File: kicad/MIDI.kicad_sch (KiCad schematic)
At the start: 24 parts, among them J11 AudioJack2, J12 AudioJack2, J13 AudioJack2, J5 DIN-5_180degree, J6 DIN-5_180degree, J7 DIN-5_180degree, J9 Conn_01x07_Socket, U5 H11L1

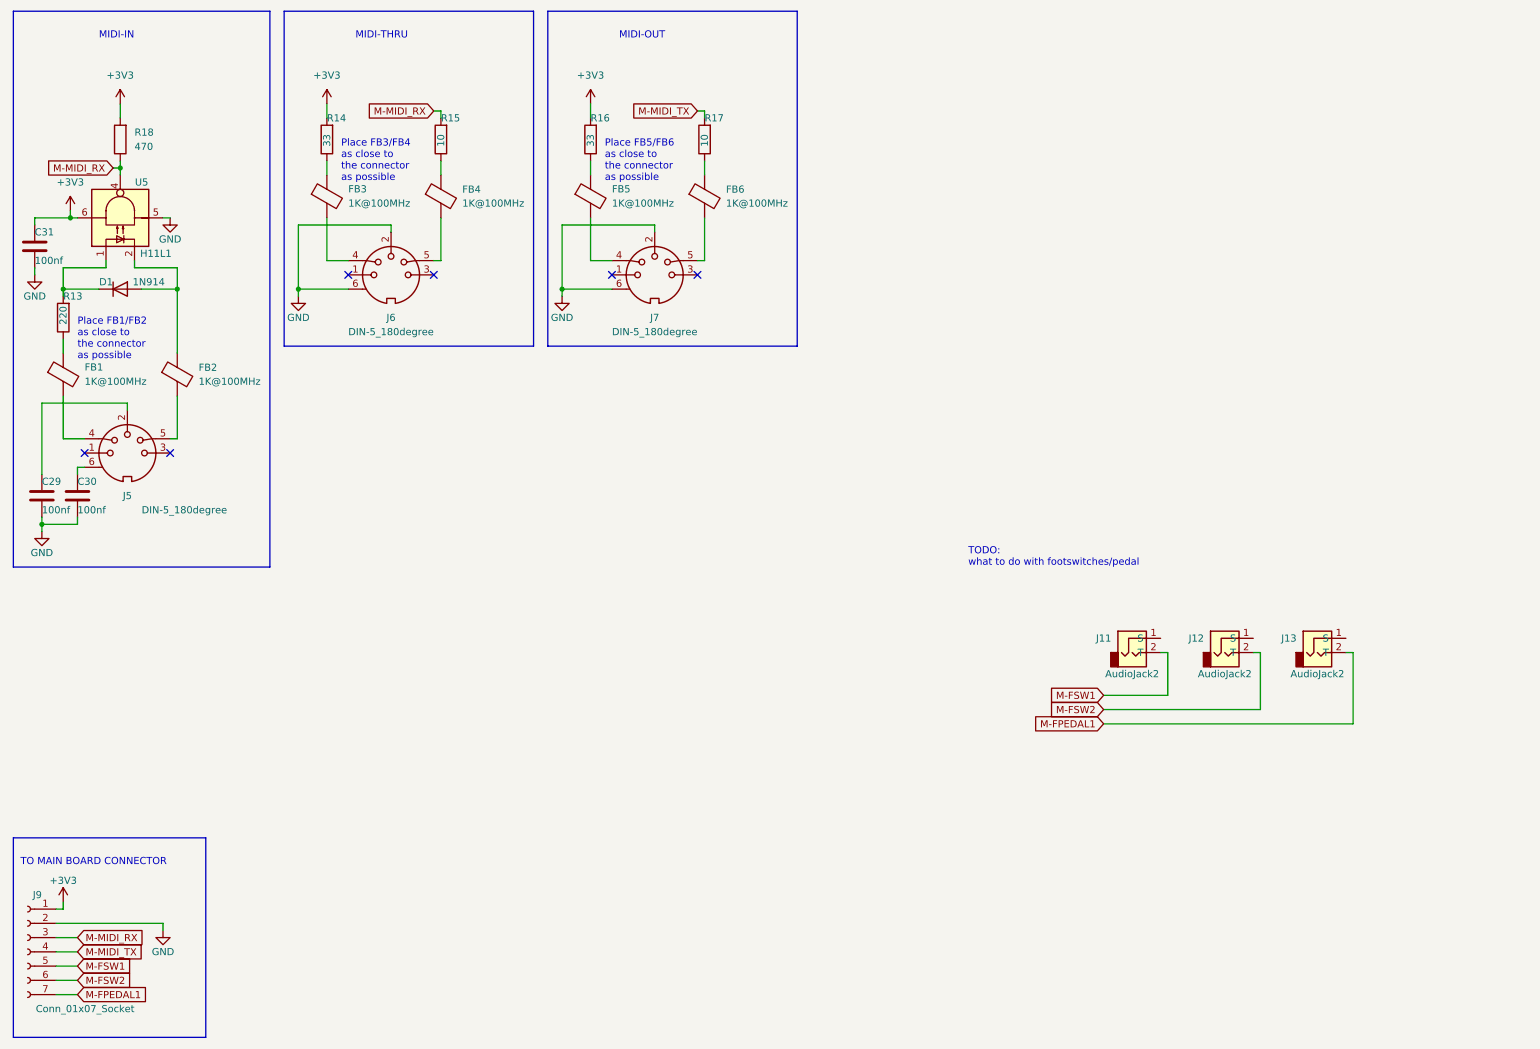
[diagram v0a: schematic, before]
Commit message: continued work on fader pcb and redid all references more logicly
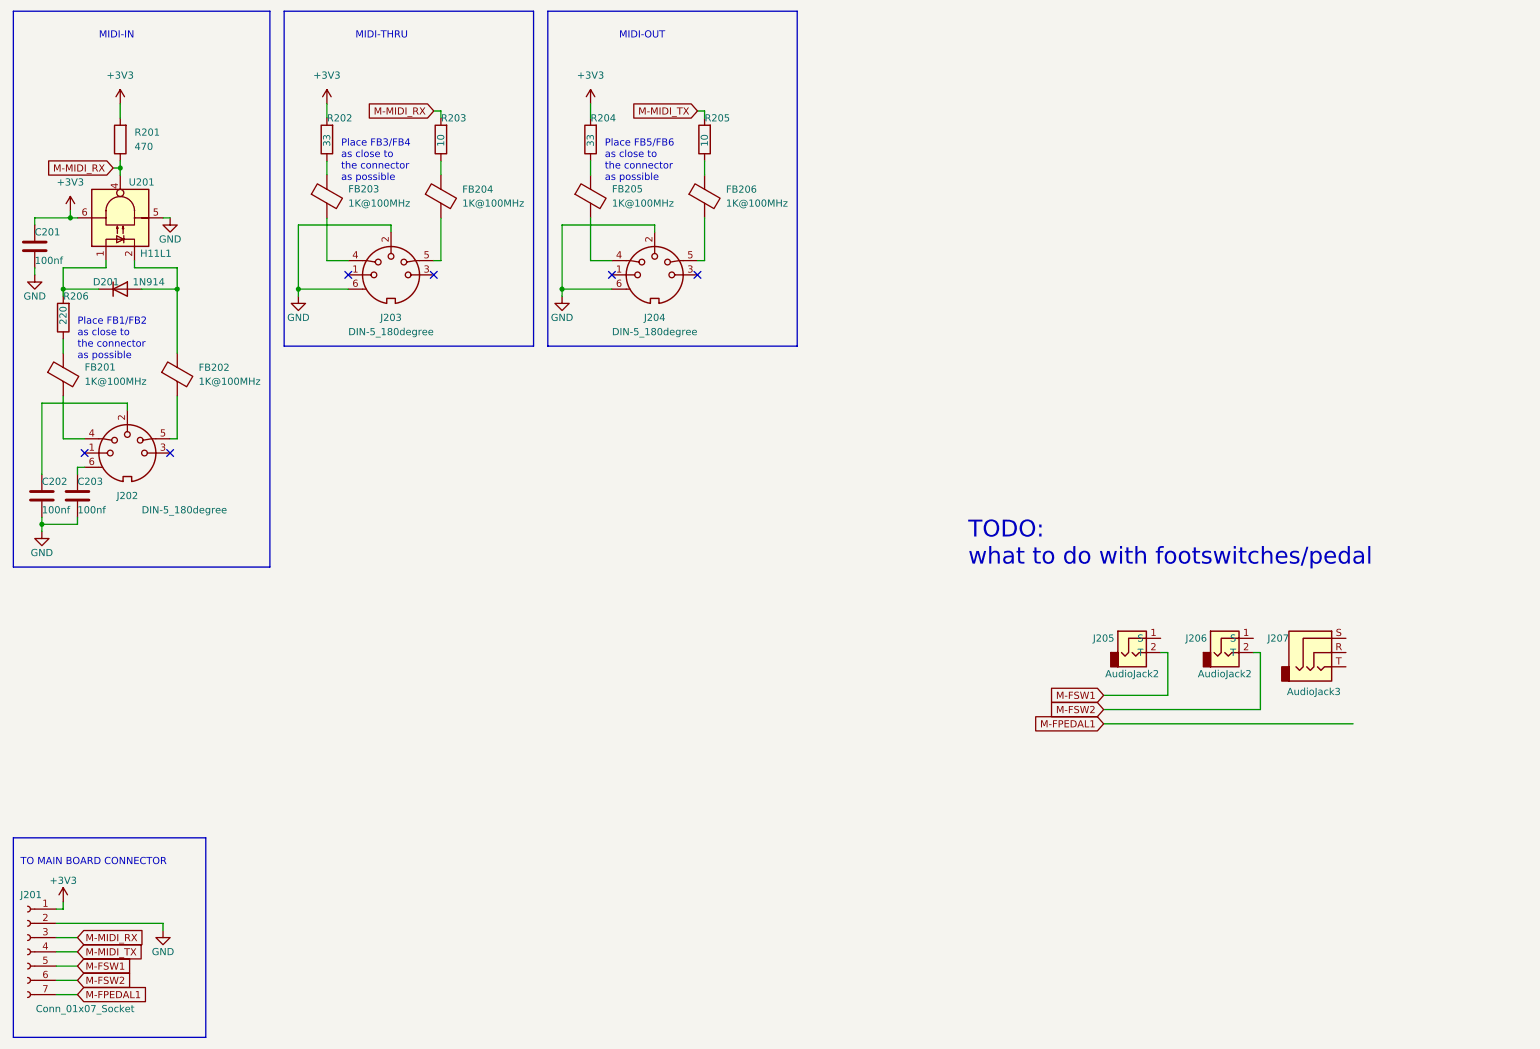
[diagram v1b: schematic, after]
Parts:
- J207: renamed from J13; value AudioJack2 -> AudioJack3; symbol Connector_Audio:AudioJack2 -> Connector_Audio:AudioJack3
- renumbered C31 to C201, C29 to C202, C30 to C203, D1 to D201, FB1 to FB201, FB2 to FB202, FB3 to FB203, FB4 to FB204, FB5 to FB205, FB6 to FB206, J9 to J201, J5 to J202, J6 to J203, J7 to J204, J11 to J205, J12 to J206, R18 to R201, R14 to R202, R15 to R203, R16 to R204, R17 to R205, R13 to R206, U5 to U201
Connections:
- net M-FPEDAL1: no longer J207.2 (T)
